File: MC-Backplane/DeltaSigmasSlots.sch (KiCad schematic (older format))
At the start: 0 parts

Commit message: added reverse polarity protection circuit and fuse
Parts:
- added U? (x2): 86094328314755V1LF, symbol MC-Backplane:86094328314755V1LF
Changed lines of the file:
@@
 $Descr A4 11693 8268
 encoding utf-8
-Sheet 1 5
+Sheet 3 5
 Title ""
 Date ""
@@
 Comment4 ""
 $EndDescr
+$Comp
+L MC-Backplane:86094328314755V1LF U?
+U 1 1 61F316BD
+P 3150 4700
+F 0 "U?" H 3150 6517 50  0000 C CNN
+F 1 "86094328314755V1LF" H 3150 6426 50  0000 C CNN
+F 2 "" H 3150 4700 50  0001 C CNN
+F 3 "" H 3150 4700 50  0001 C CNN
+	1    3150 4700
+	1    0    0    -1
+$EndComp
+$Comp
+L MC-Backplane:86094328314755V1LF U?
+U 1 1 61F33A0E
+P 7600 4800
+F 0 "U?" H 7600 6617 50  0000 C CNN
+F 1 "86094328314755V1LF" H 7600 6526 50  0000 C CNN
+F 2 "" H 7600 4800 50  0001 C CNN
+F 3 "" H 7600 4800 50  0001 C CNN
+	1    7600 4800
+	1    0    0    -1
+$EndComp
 $EndSCHEMATC

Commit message: Add files via upload
updating net names and wires
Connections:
- net 24V: now reaches U?.1 (Pin_1)
- net 24V: now also U?.1 (Pin_1)
- net GND: now reaches U?.10 (Pin_10)
- net GND: now also U?.10 (Pin_10), U?.12 (Pin_12), U?.12 (Pin_12), U?.14 (Pin_14), U?.14 (Pin_14), U?.15 (Pin_15), U?.15 (Pin_15), U?.16 (Pin_16), U?.16 (Pin_16), U?.18 (Pin_18), U?.18 (Pin_18), U?.2 (Pin_2), U?.2 (Pin_2), U?.20 (Pin_20), U?.20 (Pin_20), U?.22 (Pin_22), U?.22 (Pin_22), U?.24 (Pin_24), U?.24 (Pin_24), U?.26 (Pin_26), U?.26 (Pin_26), U?.28 (Pin_28), U?.28 (Pin_28), U?.30 (Pin_30), U?.30 (Pin_30), U?.31 (Pin_31), U?.31 (Pin_31), U?.32 (Pin_32), U?.32 (Pin_32), U?.4 (Pin_4), U?.4 (Pin_4), U?.6 (Pin_6), U?.6 (Pin_6), U?.8 (Pin_8), U?.8 (Pin_8)
- net DS_Epwm_A3: now reaches U?.11 (Pin_11)
- net DS_Epwm_A4: now reaches U?.13 (Pin_13)
- net CLOCK: now reaches U?.17 (Pin_17)
- net CLOCK: now also U?.17 (Pin_17)
- net SAFE_STATE_FLAG: now reaches U?.19 (Pin_19)
- net SAFE_STATE_FLAG: now also U?.21 (Pin_21)
- net EMITTER_ENABLE: now reaches U?.21 (Pin_21)
- net EMITTER_ENABLE: now also U?.19 (Pin_19)
- net DS_GPIO_D_A1: now reaches U?.23 (Pin_23)
- net DS_GPIO_D_A2: now reaches U?.25 (Pin_25)
- net DS_GPIO_D_A3: now reaches U?.27 (Pin_27)
- net DS_GPIO_D_A4: now reaches U?.29 (Pin_29)
- net DS_SD_A: now reaches U?.3 (Pin_3)
- net DS_Clk_A: now reaches U?.5 (Pin_5)
- net DS_Epwm_A1: now reaches U?.7 (Pin_7)
- net DS_Epwm_A2: now reaches U?.9 (Pin_9)
- net DS_Epwm_B3: now reaches U?.11 (Pin_11)
- net DS_Epwm_B4: now reaches U?.13 (Pin_13)
- net DS_GPIO_D_B1: now reaches U?.23 (Pin_23)
- net DS_GPIO_D_B2: now reaches U?.25 (Pin_25)
- net DS_GPIO_D_B3: now reaches U?.27 (Pin_27)
- net DS_GPIO_D_B4: now reaches U?.29 (Pin_29)
- net DS_SD_B: now reaches U?.3 (Pin_3)
- net DS_Clk_B: now reaches U?.5 (Pin_5)
- net DS_Epwm_B1: now reaches U?.7 (Pin_7)
- net DS_Epwm_B2: now reaches U?.9 (Pin_9)
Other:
- note added: "A"
- note added: "B"
- note added: "Delta Sigma"
- note added: "all inputs, 4 clk and 4 data"
- note added: "change the naming scheme of these"
- note added: "slot 7"
- note added: "slot 8"

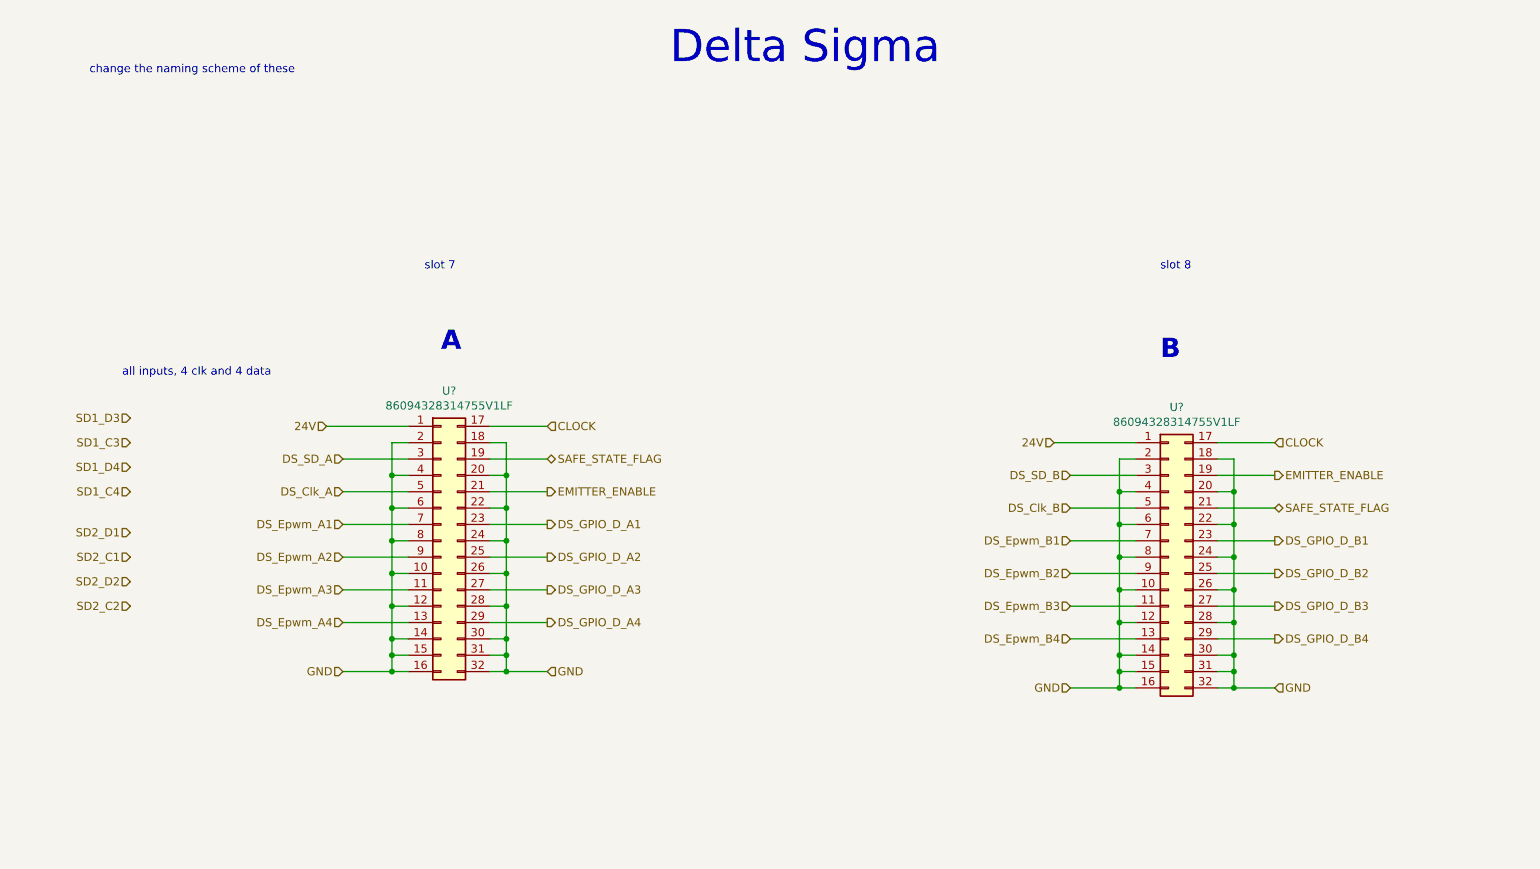
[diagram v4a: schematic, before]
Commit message: Signal naming cleanup/ dsp pin pairing
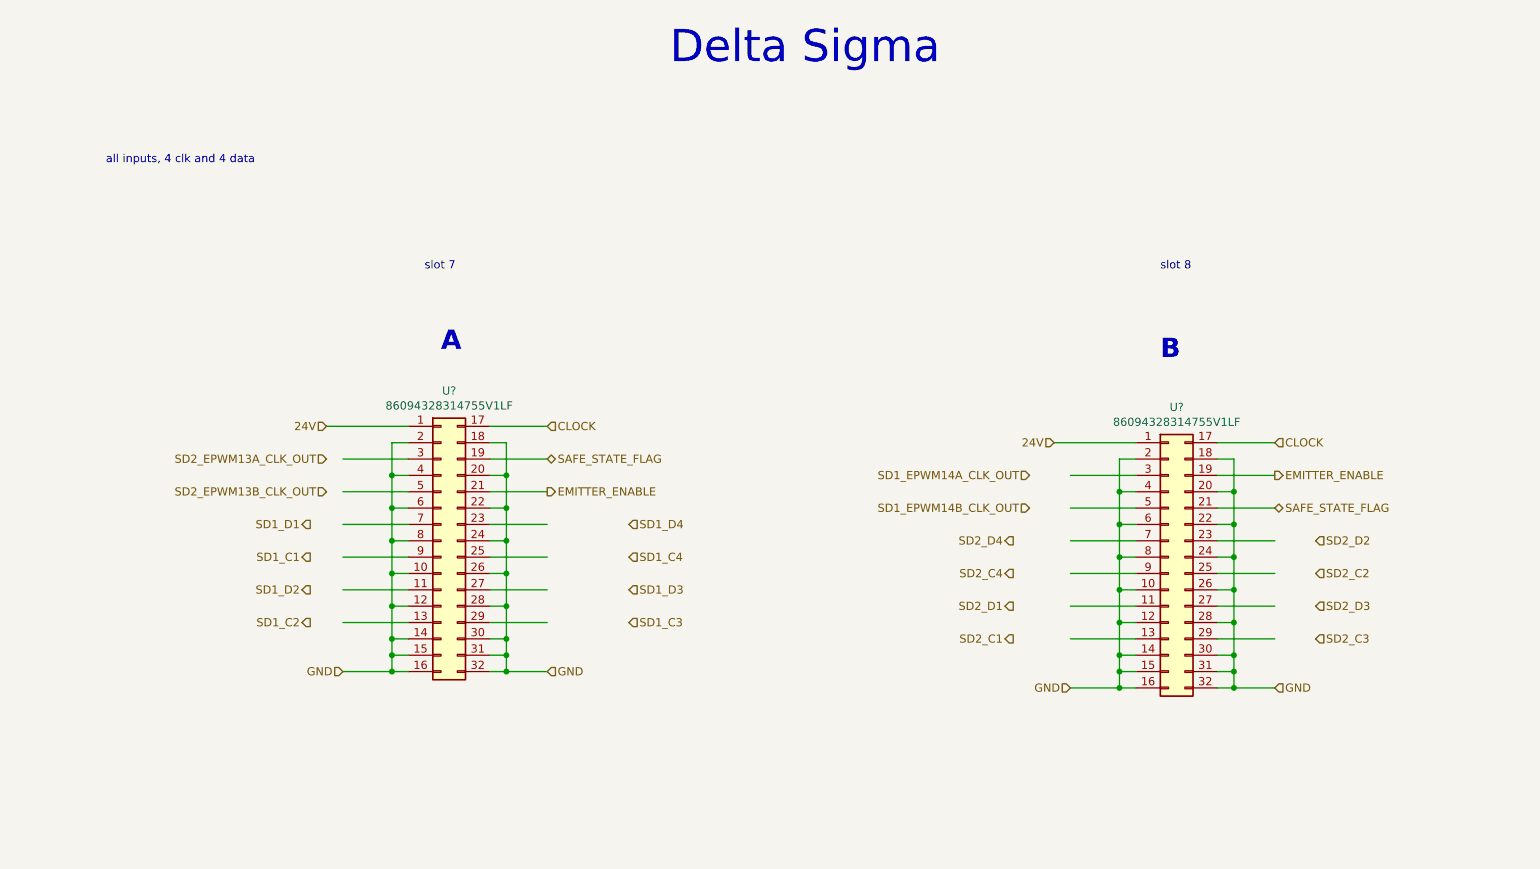
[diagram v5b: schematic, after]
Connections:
- net labels added: SD1_C1, SD1_C2, SD1_D1, SD1_D2, SD1_EPWM14A_CLK_OUT, SD1_EPWM14B_CLK_OUT, SD2_C3, SD2_C4, SD2_D3, SD2_D4, SD2_EPWM13A_CLK_OUT, SD2_EPWM13B_CLK_OUT
- net labels removed: DS_Clk_A, DS_Clk_B, DS_Epwm_A1, DS_Epwm_A2, DS_Epwm_A3, DS_Epwm_A4, DS_Epwm_B1, DS_Epwm_B2, DS_Epwm_B3, DS_Epwm_B4, DS_GPIO_D_A1, DS_GPIO_D_A2, DS_GPIO_D_A3, DS_GPIO_D_A4, DS_GPIO_D_B1, DS_GPIO_D_B2, DS_GPIO_D_B3, DS_GPIO_D_B4, DS_SD_A, DS_SD_B
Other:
- note removed: "change the naming scheme of these"
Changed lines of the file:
@@
 $Descr A4 11693 8268
 encoding utf-8
-Sheet 5 7
+Sheet 3 7
 Title ""
 Date ""
@@
 	1    0    0    -1
 $EndComp
-Text HLabel 2500 3700 0    50   Input ~ 0
-DS_Epwm_A1
 Text Notes 3100 2650 0    118  ~ 24
 A
 Text Notes 7500 2700 0    118  ~ 24
 B
-Text HLabel 2500 3900 0    50   Input ~ 0
-DS_Epwm_A2
-Text HLabel 2500 4100 0    50   Input ~ 0
-DS_Epwm_A3
-Text HLabel 2500 4300 0    50   Input ~ 0
-DS_Epwm_A4
-Text HLabel 6950 3800 0    50   Input ~ 0
-DS_Epwm_B1
-Text HLabel 6950 4000 0    50   Input ~ 0
-DS_Epwm_B2
-Text HLabel 6950 4200 0    50   Input ~ 0
-DS_Epwm_B3
-Text HLabel 6950 4400 0    50   Input ~ 0
-DS_Epwm_B4
-Text HLabel 3750 3700 2    50   Output ~ 0
-DS_GPIO_D_A1
-Text HLabel 3750 3900 2    50   Output ~ 0
-DS_GPIO_D_A2
-Text HLabel 3750 4100 2    50   Output ~ 0
-DS_GPIO_D_A3
-Text HLabel 3750 4300 2    50   Output ~ 0
-DS_GPIO_D_A4
-Text HLabel 8200 3800 2    50   Output ~ 0
-DS_GPIO_D_B1
-Text HLabel 8200 4000 2    50   Output ~ 0
-DS_GPIO_D_B2
-Text HLabel 8200 4200 2    50   Output ~ 0
-DS_GPIO_D_B3
-Text HLabel 8200 4400 2    50   Output ~ 0
-DS_GPIO_D_B4
 Text HLabel 3750 3100 2    50   Input ~ 0
 CLOCK
@@
 Text HLabel 8200 3400 2    50   Output ~ 0
 EMITTER_ENABLE
-Text HLabel 2500 3500 0    50   Input ~ 0
-DS_Clk_A
-Text HLabel 6950 3400 0    50   Input ~ 0
-DS_SD_B
-Text HLabel 6950 3600 0    50   Input ~ 0
-DS_Clk_B
 Wire Wire Line
 	2900 3100 2400 3100
@@
 Wire Wire Line
 	7850 3300 7950 3300
-Text Notes 950  950  0    50   ~ 0
-change the naming scheme of these
 Text Notes 3000 2150 0    50   ~ 0
 slot 7
 Text Notes 7500 2150 0    50   ~ 0
 slot 8
-Text HLabel 2500 3300 0    50   Input ~ 0
-DS_SD_A
-Text HLabel 1200 3050 0    50   Input ~ 0
+Text HLabel 4250 4100 2    50   Input ~ 0
 SD1_D3
-Text HLabel 1200 3200 0    50   Input ~ 0
+Text HLabel 4250 4300 2    50   Input ~ 0
 SD1_C3
-Text HLabel 1200 3350 0    50   Input ~ 0
+Text HLabel 4250 3700 2    50   Input ~ 0
 SD1_D4
-Text HLabel 1200 3500 0    50   Input ~ 0
+Text HLabel 4250 3900 2    50   Input ~ 0
 SD1_C4
-Text HLabel 1200 3750 0    50   Input ~ 0
+Text HLabel 8450 4000 2    50   Input ~ 0
+SD2_C2
+Text Notes 1050 1500 0    50   ~ 0
+all inputs, 4 clk and 4 data
+Text HLabel 8450 3800 2    50   Input ~ 0
+SD2_D2
+Text HLabel 6600 4400 0    50   Output ~ 0
+SD2_C1
+Text HLabel 6600 4200 0    50   Output ~ 0
 SD2_D1
-Text HLabel 1200 3900 0    50   Input ~ 0
-SD2_C1
-Text HLabel 1200 4050 0    50   Input ~ 0
-SD2_D2
-Text HLabel 1200 4200 0    50   Input ~ 0
-SD2_C2
-Text Notes 1150 2800 0    50   ~ 0
-all inputs, 4 clk and 4 data
+Text HLabel 2300 3700 0    50   Output ~ 0
+SD1_D1
+Text HLabel 2300 3900 0    50   Output ~ 0
+SD1_C1
+Text HLabel 2300 4100 0    50   Output ~ 0
+SD1_D2
+Text HLabel 2300 4300 0    50   Output ~ 0
+SD1_C2
+Text HLabel 8450 4400 2    50   Input ~ 0
+SD2_C3
+Text HLabel 8450 4200 2    50   Input ~ 0
+SD2_D3
+Text HLabel 6600 3800 0    50   Output ~ 0
+SD2_D4
+Text HLabel 6600 4000 0    50   Output ~ 0
+SD2_C4
+Text HLabel 6700 3400 0    50   Input ~ 0
+SD1_EPWM14A_CLK_OUT
+Text HLabel 6700 3600 0    50   Input ~ 0
+SD1_EPWM14B_CLK_OUT
+Text HLabel 2400 3300 0    50   Input ~ 0
+SD2_EPWM13A_CLK_OUT
+Text HLabel 2400 3500 0    50   Input ~ 0
+SD2_EPWM13B_CLK_OUT
 $EndSCHEMATC

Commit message: DSP interface pin out
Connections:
- net labels added: GPIO12_EMITTER_ENABLE, GPIO13_SAFE_STATE_FLAG
- net labels removed: EMITTER_ENABLE, SAFE_STATE_FLAG
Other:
- note removed: "A"
- note removed: "B"
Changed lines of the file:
@@
 	1    0    0    -1
 $EndComp
-Text Notes 3100 2650 0    118  ~ 24
-A
-Text Notes 7500 2700 0    118  ~ 24
-B
 Text HLabel 3750 3100 2    50   Input ~ 0
 CLOCK
 Text HLabel 8200 3200 2    50   Input ~ 0
 CLOCK
-Text HLabel 3750 4600 2    50   Input ~ 0
+Text HLabel 3500 4825 2    50   Input ~ 0
 GND
-Text HLabel 8200 4700 2    50   Input ~ 0
+Text HLabel 7950 5000 2    50   Input ~ 0
 GND
 Text HLabel 2400 3100 0    50   Input ~ 0
@@
 Text HLabel 6850 3200 0    50   Input ~ 0
 24V
-Text HLabel 3750 3300 2    50   BiDi ~ 0
-SAFE_STATE_FLAG
-Text HLabel 8200 3600 2    50   BiDi ~ 0
-SAFE_STATE_FLAG
 Text Notes 4500 900  0    197  ~ 0
 Delta Sigma
-Text HLabel 3750 3500 2    50   Output ~ 0
-EMITTER_ENABLE
-Text HLabel 8200 3400 2    50   Output ~ 0
-EMITTER_ENABLE
 Wire Wire Line
 	2900 3100 2400 3100
@@
 	3400 3100 3750 3100
 Wire Wire Line
-	3400 3300 3750 3300
+	3400 3300 3500 3300
 Wire Wire Line
 	3400 3500 3750 3500
@@
 Wire Wire Line
 	3750 4300 3400 4300
-Wire Wire Line
-	3750 4600 3500 4600
-Text HLabel 2500 4600 0    50   Input ~ 0
+Text HLabel 2800 4825 0    50   Input ~ 0
 GND
 Wire Wire Line
 	2900 3200 2800 3200
 Wire Wire Line
-	2800 3200 2800 3400
-Wire Wire Line
-	2500 4600 2800 4600
-Connection ~ 2800 4600
-Wire Wire Line
-	2800 4600 2900 4600
-Wire Wire Line
-	3500 3200 3500 3400
-Connection ~ 3500 4600
-Wire Wire Line
-	3500 4600 3400 4600
-Wire Wire Line
-	2900 3300 2500 3300
+	2800 3200 2800 3300
+Wire Wire Line
+	3500 3200 3500 3300
+Wire Wire Line
+	2900 3300 2800 3300
 Wire Wire Line
 	2900 3400 2800 3400
@@
 Wire Wire Line
 	2900 4400 2800 4400
-Connection ~ 2800 4400
-Wire Wire Line
-	2800 4400 2800 4500
-Wire Wire Line
-	2900 4500 2800 4500
-Connection ~ 2800 4500
-Wire Wire Line
-	2800 4500 2800 4600
 Wire Wire Line
 	3400 4400 3500 4400
-Connection ~ 3500 4400
-Wire Wire Line
-	3500 4400 3500 4500
-Wire Wire Line
-	3400 4500 3500 4500
-Connection ~ 3500 4500
-Wire Wire Line
-	3500 4500 3500 4600
+Wire Wire Line
+	3400 4500 3750 4500
 Wire Wire Line
 	7350 3200 6850 3200
@@
 	7350 3300 7250 3300
 Wire Wire Line
-	7250 3300 7250 3500
-Wire Wire Line
-	6950 4700 7250 4700
-Connection ~ 7250 4700
-Wire Wire Line
-	7250 4700 7350 4700
-Wire Wire Line
-	7350 3400 6950 3400
+	7250 3300 7250 3400
+Wire Wire Line
+	7350 3400 7250 3400
 Wire Wire Line
 	7350 3500 7250 3500
@@
 Wire Wire Line
 	7350 4500 7250 4500
-Connection ~ 7250 4500
-Wire Wire Line
-	7250 4500 7250 4600
-Wire Wire Line
-	7350 4600 7250 4600
-Connection ~ 7250 4600
-Wire Wire Line
-	7250 4600 7250 4700
-Text HLabel 6950 4700 0    50   Input ~ 0
+Text HLabel 7250 5000 0    50   Input ~ 0
 GND
 Wire Wire Line
@@
 	7850 3200 8200 3200
 Wire Wire Line
-	7850 3400 8200 3400
+	7850 3400 7950 3400
 Wire Wire Line
 	7850 3600 8200 3600
@@
 	7850 4200 8200 4200
 Wire Wire Line
-	8200 4400 7850 4400
-Wire Wire Line
-	8200 4700 7950 4700
-Wire Wire Line
-	7950 3300 7950 3500
-Connection ~ 7950 4700
-Wire Wire Line
-	7950 4700 7850 4700
-Wire Wire Line
-	7850 4500 7950 4500
-Connection ~ 7950 4500
-Wire Wire Line
-	7950 4500 7950 4600
-Wire Wire Line
-	7850 4600 7950 4600
-Connection ~ 7950 4600
-Wire Wire Line
-	7950 4600 7950 4700
+	7950 3300 7950 3400
 Wire Wire Line
 	7850 3500 7950 3500
@@
 Wire Wire Line
 	7850 4100 7950 4100
-Connection ~ 7950 4100
-Wire Wire Line
-	7950 4100 7950 4300
-Wire Wire Line
-	7850 4300 7950 4300
-Connection ~ 7950 4300
-Wire Wire Line
-	7950 4300 7950 4500
 Wire Wire Line
 	7850 3300 7950 3300
@@
 Text Notes 7500 2150 0    50   ~ 0
 slot 8
-Text HLabel 4250 4100 2    50   Input ~ 0
+Text HLabel 3750 4100 2    50   Input ~ 0
 SD1_D3
-Text HLabel 4250 4300 2    50   Input ~ 0
+Text HLabel 3750 4300 2    50   Input ~ 0
 SD1_C3
-Text HLabel 4250 3700 2    50   Input ~ 0
+Text HLabel 3750 3700 2    50   Input ~ 0
 SD1_D4
-Text HLabel 4250 3900 2    50   Input ~ 0
+Text HLabel 3750 3900 2    50   Input ~ 0
 SD1_C4
-Text HLabel 8450 4000 2    50   Input ~ 0
+Text HLabel 8200 4000 2    50   Input ~ 0
 SD2_C2
 Text Notes 1050 1500 0    50   ~ 0
 all inputs, 4 clk and 4 data
-Text HLabel 8450 3800 2    50   Input ~ 0
+Text HLabel 8200 3800 2    50   Input ~ 0
 SD2_D2
-Text HLabel 6600 4400 0    50   Output ~ 0
+Text HLabel 6950 4400 0    50   Output ~ 0
 SD2_C1
-Text HLabel 6600 4200 0    50   Output ~ 0
+Text HLabel 6950 4200 0    50   Output ~ 0
 SD2_D1
-Text HLabel 2300 3700 0    50   Output ~ 0
+Text HLabel 2500 3700 0    50   Output ~ 0
 SD1_D1
-Text HLabel 2300 3900 0    50   Output ~ 0
+Text HLabel 2500 3900 0    50   Output ~ 0
 SD1_C1
-Text HLabel 2300 4100 0    50   Output ~ 0
+Text HLabel 2500 4100 0    50   Output ~ 0
 SD1_D2
-Text HLabel 2300 4300 0    50   Output ~ 0
+Text HLabel 2500 4300 0    50   Output ~ 0
 SD1_C2
-Text HLabel 8450 4400 2    50   Input ~ 0
+Text HLabel 8200 4400 2    50   Input ~ 0
 SD2_C3
-Text HLabel 8450 4200 2    50   Input ~ 0
+Text HLabel 8200 4200 2    50   Input ~ 0
 SD2_D3
-Text HLabel 6600 3800 0    50   Output ~ 0
+Text HLabel 6950 3800 0    50   Output ~ 0
 SD2_D4
-Text HLabel 6600 4000 0    50   Output ~ 0
+Text HLabel 6950 4000 0    50   Output ~ 0
 SD2_C4
-Text HLabel 6700 3400 0    50   Input ~ 0
+Text HLabel 2500 3500 0    50   Input ~ 0
 SD1_EPWM14A_CLK_OUT
-Text HLabel 6700 3600 0    50   Input ~ 0
+Text HLabel 3750 3500 2    50   Input ~ 0
 SD1_EPWM14B_CLK_OUT
-Text HLabel 2400 3300 0    50   Input ~ 0
+Text HLabel 6950 3600 0    50   Input ~ 0
 SD2_EPWM13A_CLK_OUT
-Text HLabel 2400 3500 0    50   Input ~ 0
+Text HLabel 8200 3600 2    50   Input ~ 0
 SD2_EPWM13B_CLK_OUT
+Connection ~ 7950 3400
+Wire Wire Line
+	7950 3400 7950 3500
+Wire Wire Line
+	7850 4700 7950 4700
+Wire Wire Line
+	7950 4100 7950 4300
+Connection ~ 7950 4100
+Connection ~ 7950 4700
+Wire Wire Line
+	7950 4700 7950 5000
+Wire Wire Line
+	7850 4300 7950 4300
+Connection ~ 7950 4300
+Wire Wire Line
+	7950 4300 7950 4500
+Wire Wire Line
+	7850 4500 7950 4500
+Connection ~ 7950 4500
+Wire Wire Line
+	7850 4400 8200 4400
+Wire Wire Line
+	7250 5000 7250 4700
+Wire Wire Line
+	7350 4600 6950 4600
+Wire Wire Line
+	7250 4500 7250 4700
+Connection ~ 7250 4500
+Connection ~ 7250 4700
+Wire Wire Line
+	7250 4700 7350 4700
+Text HLabel 2500 4500 0    50   BiDi ~ 0
+GPIO13_SAFE_STATE_FLAG
+Text HLabel 3750 4500 2    50   Input ~ 0
+GPIO12_EMITTER_ENABLE
+Text HLabel 6950 4600 0    50   BiDi ~ 0
+GPIO13_SAFE_STATE_FLAG
+Text HLabel 8200 4600 2    50   Input ~ 0
+GPIO12_EMITTER_ENABLE
+Wire Wire Line
+	7950 4500 7950 4700
+Wire Wire Line
+	2800 4825 2800 4600
+Wire Wire Line
+	3400 4600 3500 4600
+Wire Wire Line
+	2900 4500 2500 4500
+Wire Wire Line
+	2800 4400 2800 4600
+Connection ~ 2800 4400
+Connection ~ 2800 4600
+Wire Wire Line
+	2800 4600 2900 4600
+Wire Wire Line
+	3500 4400 3500 4600
+Connection ~ 3500 4400
+Connection ~ 3500 4600
+Wire Wire Line
+	3500 4600 3500 4825
+Connection ~ 2800 3300
+Wire Wire Line
+	2800 3300 2800 3400
+Connection ~ 3500 3300
+Wire Wire Line
+	3500 3300 3500 3400
+Wire Wire Line
+	7850 4600 8200 4600
+Connection ~ 7250 3400
+Wire Wire Line
+	7250 3400 7250 3500
 $EndSCHEMATC

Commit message: beginning layout
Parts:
- removed U? (x2): 86094328314755V1LF, symbol MC-Backplane:86094328314755V1LF
- added J21, J22: 86094328314755V1LF, 86094328314755V1LF, symbol Existing_IC_Models:86094328314755V1LF
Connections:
- net 24V: now also J21.A1, J22.A1
- net CLOCK: now also J21.C1, J22.C1
- net GND: now also J21.A10, J21.A12, J21.A14, J21.A16, J21.A2, J21.A3, J21.A4, J21.A6, J21.A8, J21.B1, J21.B10, J21.B11, J21.B12, J21.B13, J21.B14, J21.B15, J21.B16, J21.B2, J21.B3, J21.B4, J21.B5, J21.B6, J21.B7, J21.B8, J21.B9, J21.C10, J21.C12, J21.C14, J21.C16, J21.C2, J21.C3, J21.C4, J21.C6, J21.C8, J22.A10, J22.A12, J22.A14, J22.A16, J22.A2, J22.A3, J22.A4, J22.A6, J22.A8, J22.B1, J22.B10, J22.B11, J22.B12, J22.B13, J22.B14, J22.B15, J22.B16, J22.B2, J22.B3, J22.B4, J22.B5, J22.B6, J22.B7, J22.B8, J22.B9, J22.C10, J22.C12, J22.C14, J22.C16, J22.C2, J22.C3, J22.C4, J22.C6, J22.C8
- net GPIO12_EMITTER_ENABLE: now also J21.C15, J22.C15
- net GPIO13_SAFE_STATE_FLAG: now also J21.A15, J22.A15
- net SD1_C1: now also J21.A9
- net SD1_C2: now also J21.A13
- net SD1_C3: now also J21.C13
- net SD1_C4: now also J21.C9
- net SD1_D1: now also J21.A7
- net SD1_D2: now also J21.A11
- net SD1_D3: now also J21.C11
- net SD1_D4: now also J21.C7
- net SD1_EPWM14A_CLK_OUT: now also J21.A5
- net SD1_EPWM14B_CLK_OUT: now also J21.C5
- net SD2_C1: now also J22.A13
- net SD2_C2: now also J22.C9
- net SD2_C3: now also J22.C13
- net SD2_C4: now also J22.A9
- net SD2_D1: now also J22.A11
- net SD2_D2: now also J22.C7
- net SD2_D3: now also J22.C11
- net SD2_D4: now also J22.A7
- net SD2_EPWM13A_CLK_OUT: now also J22.A5
- net SD2_EPWM13B_CLK_OUT: now also J22.C5
